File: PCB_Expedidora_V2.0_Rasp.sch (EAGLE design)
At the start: 37 parts, among them K2 G5L, T2 2N2222

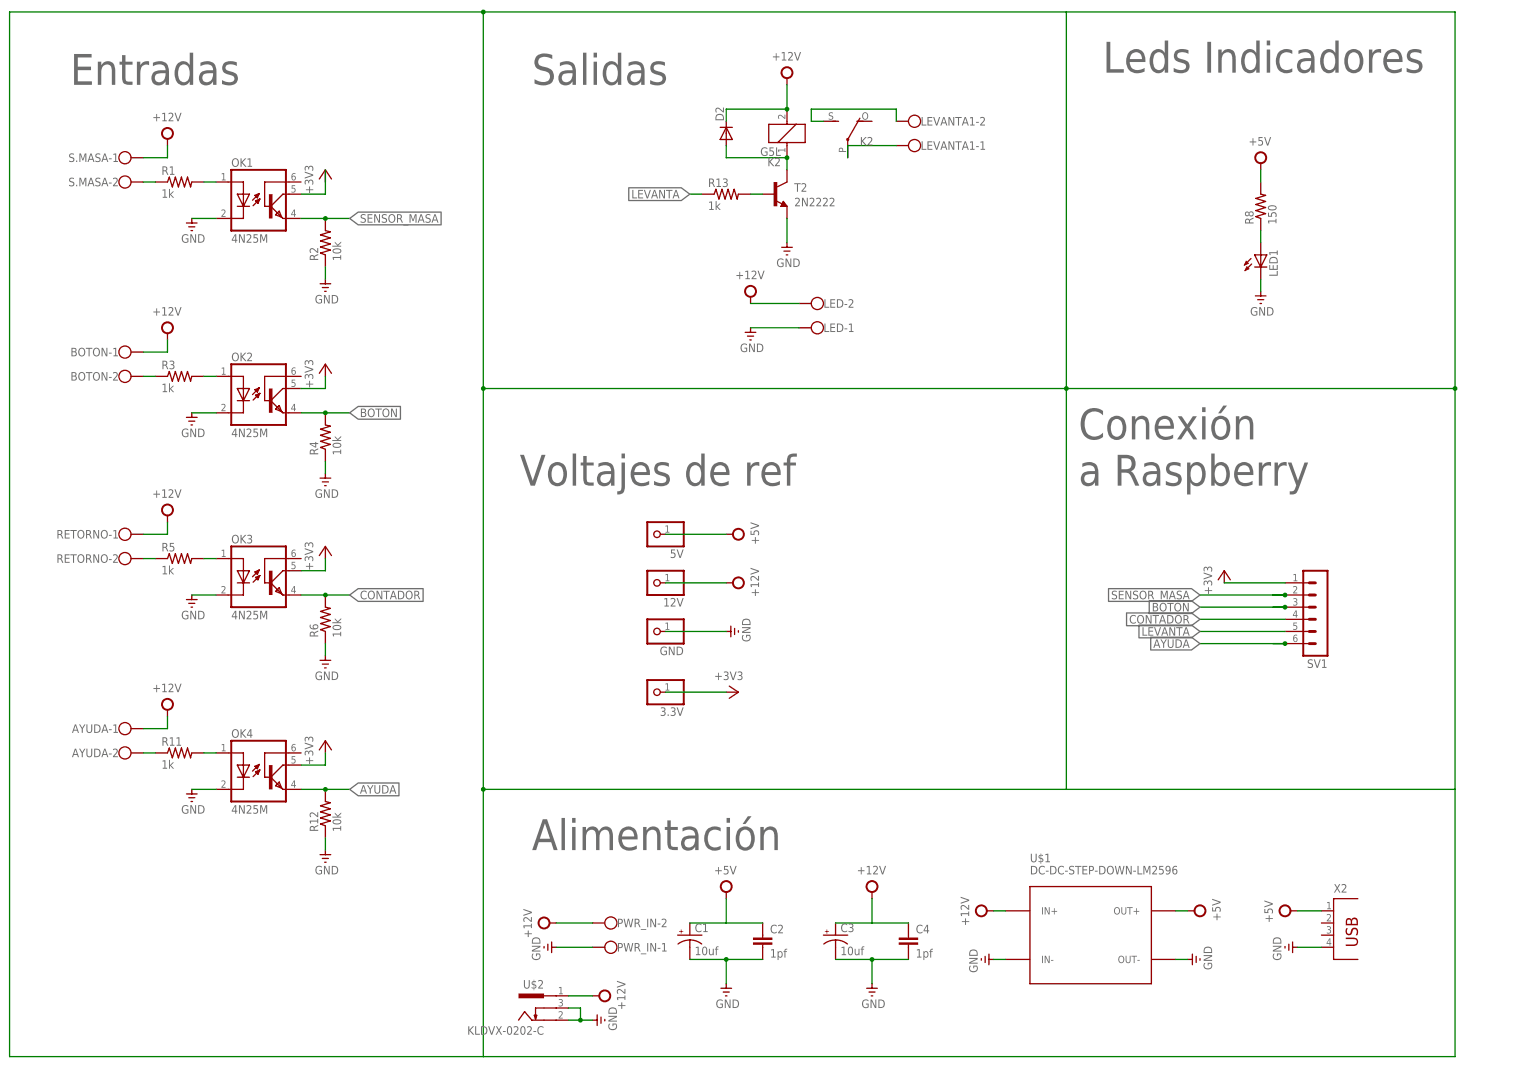
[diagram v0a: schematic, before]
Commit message: V2.1
Agrego botones y cambio de posición las borneras
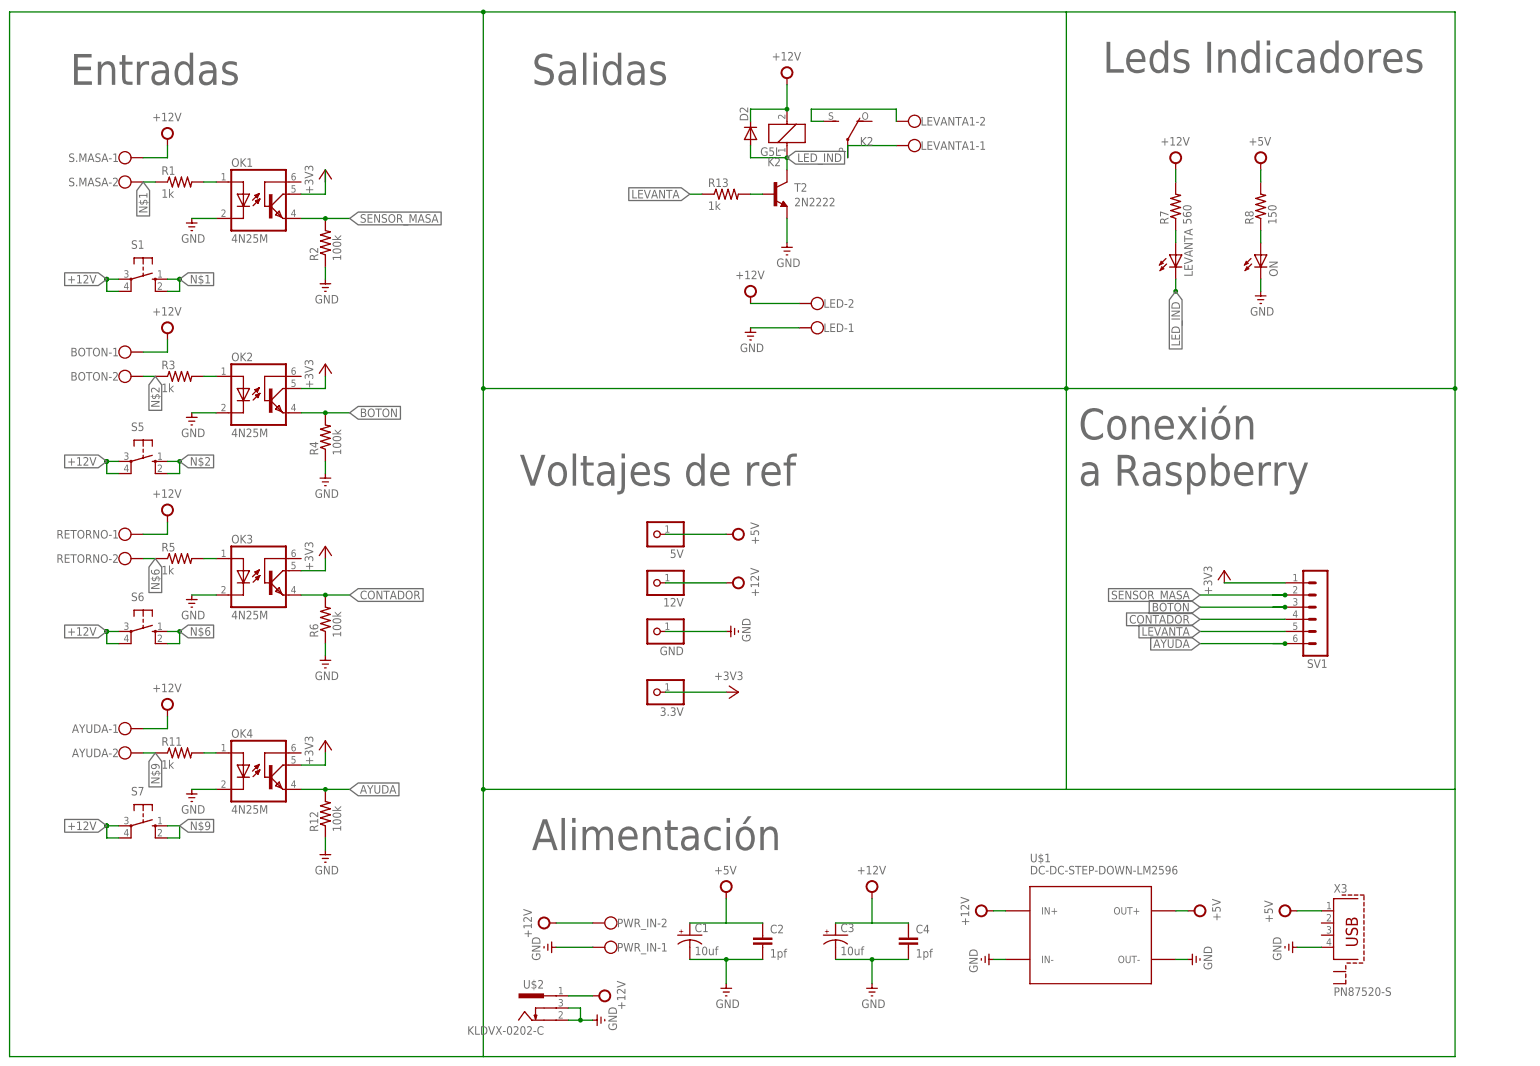
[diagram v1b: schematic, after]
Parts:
- removed X2: (no value), con-berg:PN87520
- added LEVANTA: (no value), adafruit:LED5MM
- added R7: 560, rcl:R-US_0207/7
- added S1, S5, S6, S7: (no value), switch-omron:10-XX
- added X3: PN87520-S, con-berg:PN87520-S
- R12, R2, R4, R6: value 10k -> 100k
- renumbered LED1 to ON
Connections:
- removed net N$17: D2.A, K21.1, T2.C
- new net LED_IND: D2.A, K21.1, LEVANTA.C, T2.C
- new net N$5: LEVANTA.A, R7.1
- net +12V: now also R7.2, S1.P, S1.P1, S5.P, S5.P1, S6.P, S6.P1, S7.P, S7.P1
- net +5V: now also X3.1; no longer X2.1
- net GND: now also X3.4; no longer X2.4
- net N$1: now also S1.S, S1.S1
- net N$2: now also S5.S, S5.S1
- net N$6: now also S6.S, S6.S1
- net N$9: now also S7.S, S7.S1
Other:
- moved on the sheet: D2
